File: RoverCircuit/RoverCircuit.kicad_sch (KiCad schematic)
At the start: 0 parts

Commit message: Added Servo and Stepper Motors to circuit schematic
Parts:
- added J1: PIC24_JST_1-10, Connector_JST:JST_EH_B10B-EH-A_1x10_P2.50mm_Vertical, symbol Connector_Generic:Conn_01x10
- added J2: PIC24_JST_11-20, Connector_JST:JST_EH_B10B-EH-A_1x10_P2.50mm_Vertical, symbol Connector_Generic:Conn_01x10
- added J3: Servo_JST, Connector_JST:JST_EH_B3B-EH-A_1x03_P2.50mm_Vertical, symbol Connector_Generic:Conn_01x03
- added J4: Left_Wheel_JST, symbol Connector_Generic:Conn_01x04
- added J5: Right_Wheel_JST, symbol Connector_Generic:Conn_01x04
- added M1: Motor_Servo, symbol Motor:Motor_Servo
- added M2: Left_Wheel, symbol Motor:Stepper_Motor_bipolar
- added M3: Right_Wheel, symbol Motor:Stepper_Motor_bipolar
- added MP1, MP2: MP6500, symbol Custom_Symbol_Library:MP6500_Breakout
- added Q1: NMOS, Package_TO_SOT_THT:TO-92, symbol Simulation_SPICE:NMOS
- added Q2: PMOS, Package_TO_SOT_THT:TO-92, symbol Simulation_SPICE:PMOS
- added R1, R2: 10K, Resistor_THT:R_Axial_DIN0207_L6.3mm_D2.5mm_P10.16mm_Horizontal, symbol Device:R
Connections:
- new net: M2.1, MP1. (4)
- new net: M2.2 (-), MP1. (4)
- new net: M2.3, MP1. (4)
- new net: M2.4, MP1. (4)
- new net: J4.3 (Pin_3), MP1. (4)
- new net: Q2.1 (D), R2.1
- new net: Q1.1 (D), Q2.2 (G), R1.2
- new net: J5.3 (Pin_3), MP2. (4)
- new net: M3.1, MP2. (4)
- new net: M3.2 (-), MP2. (4)
- new net: M3.3, MP2. (4)
- new net: M3.4, MP2. (4)
- new net +3V3: J2.20 (Pin_10)
- new net +5V: J3.1 (Pin_1), J3.2 (Pin_2), M1.1 (PWM), M1.2 (+), Q2.3 (S), R1.1
- new net GND: J2.19 (Pin_9), J3.3 (Pin_3), J4.4 (Pin_4), J5.4 (Pin_4), M1.3 (-), MP1. (4), MP2. (4), Q1.3 (S), R2.2
- new net Left_Wheel_DIR: J2.13 (Pin_3), J4.2 (Pin_2), MP1. (4)
- new net Left_Wheel_Step: J2.11 (Pin_1), J4.1 (Pin_1), MP1. (4)
- new net Right_Wheel_DIR: J2.12 (Pin_2), J5.2 (Pin_2), MP2. (4)
- new net Right_Wheel_Step: J1.4 (Pin_4), J5.1 (Pin_1), MP2. (4)
- new net Servo_PWM: J1.5 (Pin_5), Q1.2 (G)

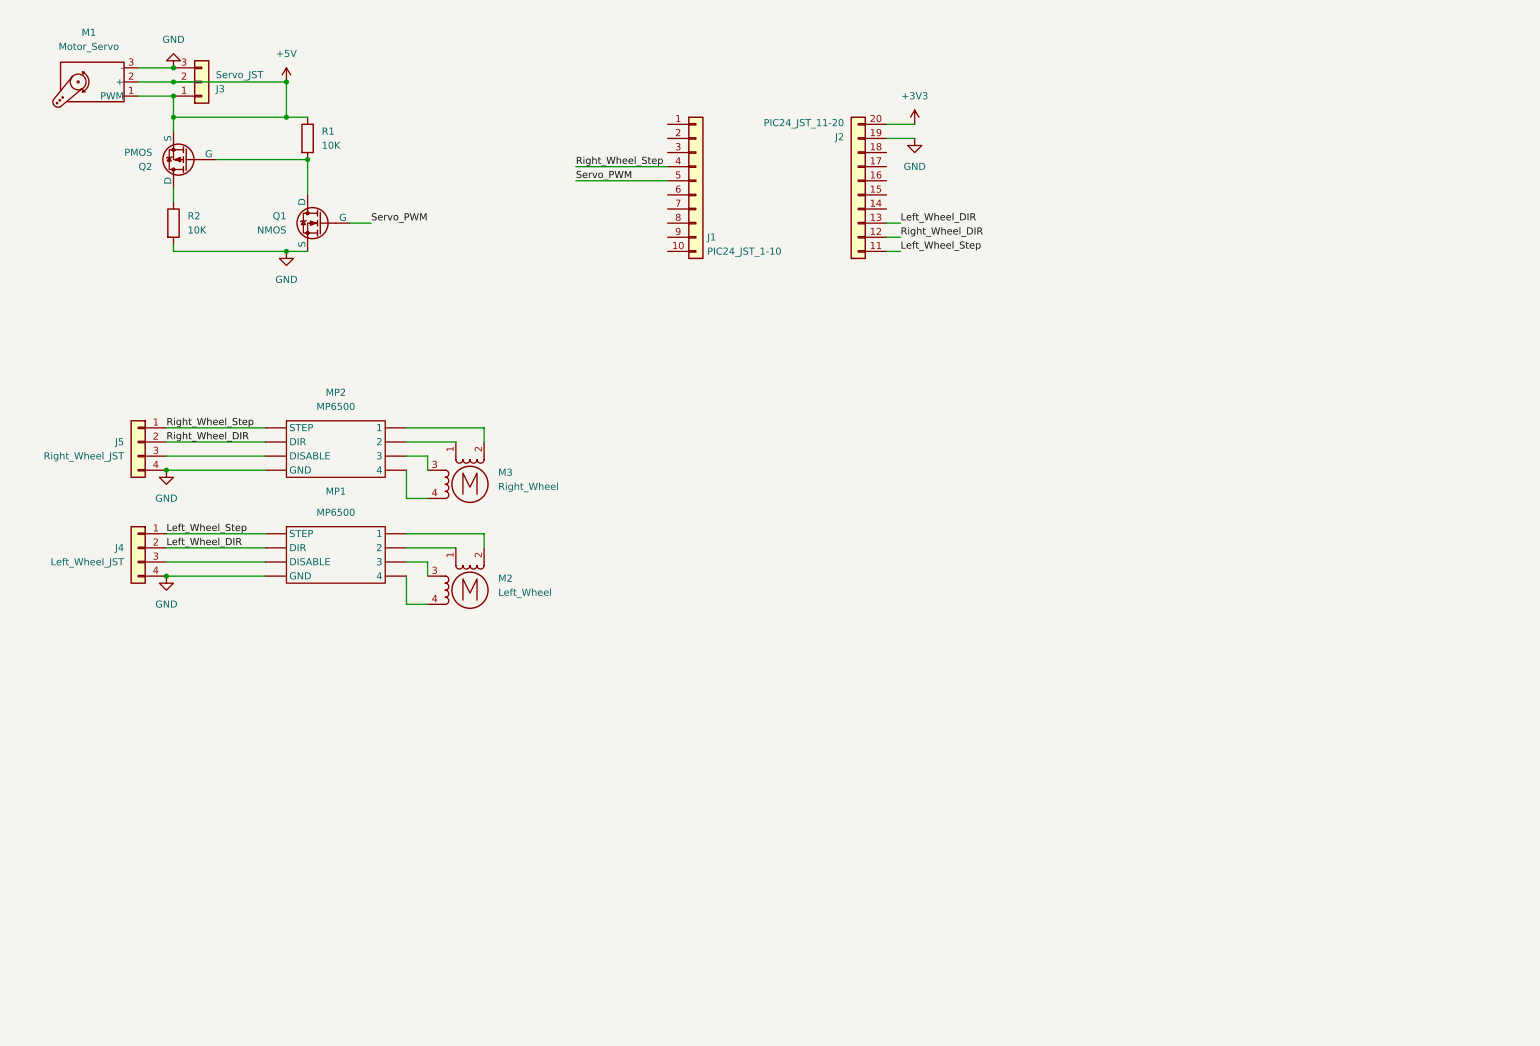
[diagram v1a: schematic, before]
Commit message: Added pinout and voltage rails
Configured pins in MPLAB and added net labels for each pin in KiCad
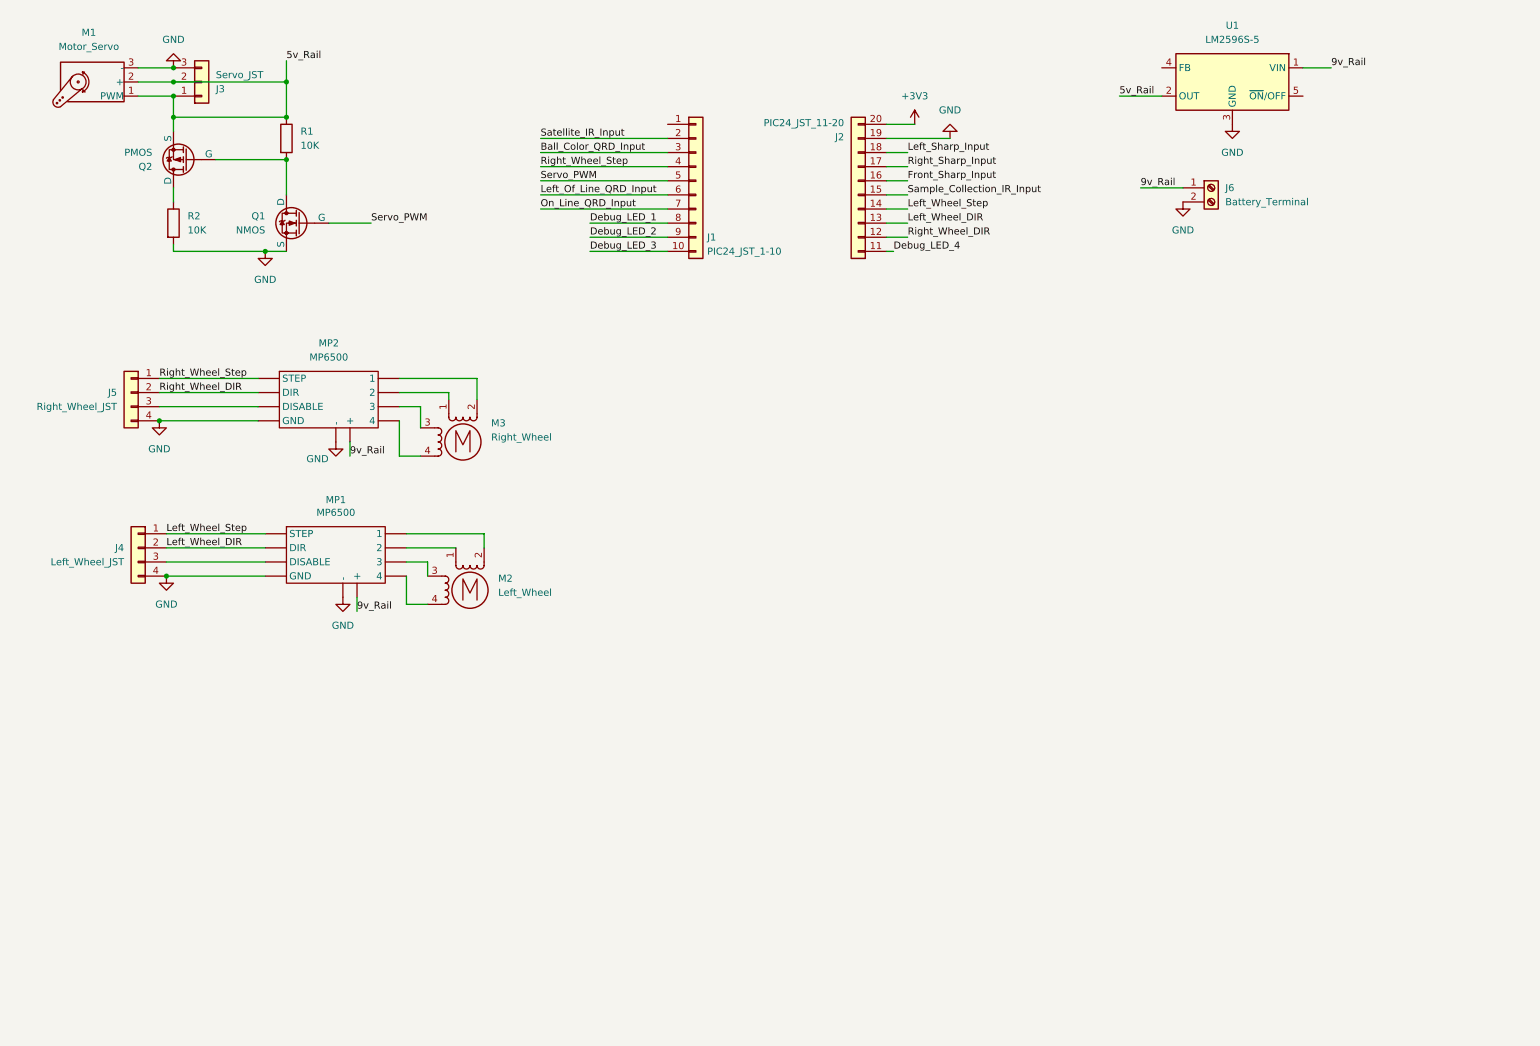
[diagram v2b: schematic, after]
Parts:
- added J6: Battery_Terminal, Connector_Phoenix_SPT:PhoenixContact_SPT_5_1-H-7.5_1x01_P7.5mm_Horizontal, symbol Connector:Screw_Terminal_01x02
- added U1: LM2596S-5, Package_TO_SOT_SMD:TO-263-5_TabPin3, symbol Regulator_Switching:LM2596S-5
- J4, J5: footprint (none) -> Connector_JST:JST_EH_B4B-EH-A_1x04_P2.50mm_Vertical
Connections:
- net GND: now also J6.2 (Pin_2), U1.3 (GND)
- net Left_Wheel_Step: now also J2.14 (Pin_4); no longer J2.11 (Pin_1)
- net Debug_LED_3: now reaches J1.10 (Pin_10)
- net Satellite_IR_Input: now reaches J1.2 (Pin_2)
- net Ball_Color_QRD_Input: now reaches J1.3 (Pin_3)
- net Left_Of_Line_QRD_Input: now reaches J1.6 (Pin_6)
- net On_Line_QRD_Input: now reaches J1.7 (Pin_7)
- net Debug_LED_1: now reaches J1.8 (Pin_8)
- net Debug_LED_2: now reaches J1.9 (Pin_9)
- net Sample_Collection_IR_Input: now reaches J2.15 (Pin_5)
- net Front_Sharp_Input: now reaches J2.16 (Pin_6)
- net Right_Sharp_Input: now reaches J2.17 (Pin_7)
- net Left_Sharp_Input: now reaches J2.18 (Pin_8)
- net +5V renamed 5v_Rail
- net 5v_Rail: now also U1.2 (OUT)
- new net 9v_Rail: J6.1 (Pin_1), MP1. (4), MP2. (4), U1.1 (VIN)
- new net Debug_LED_4: J2.11 (Pin_1)
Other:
- moved on the sheet: J5, M3, Q1, R1

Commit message: Added Sharp Sensors to KiCad
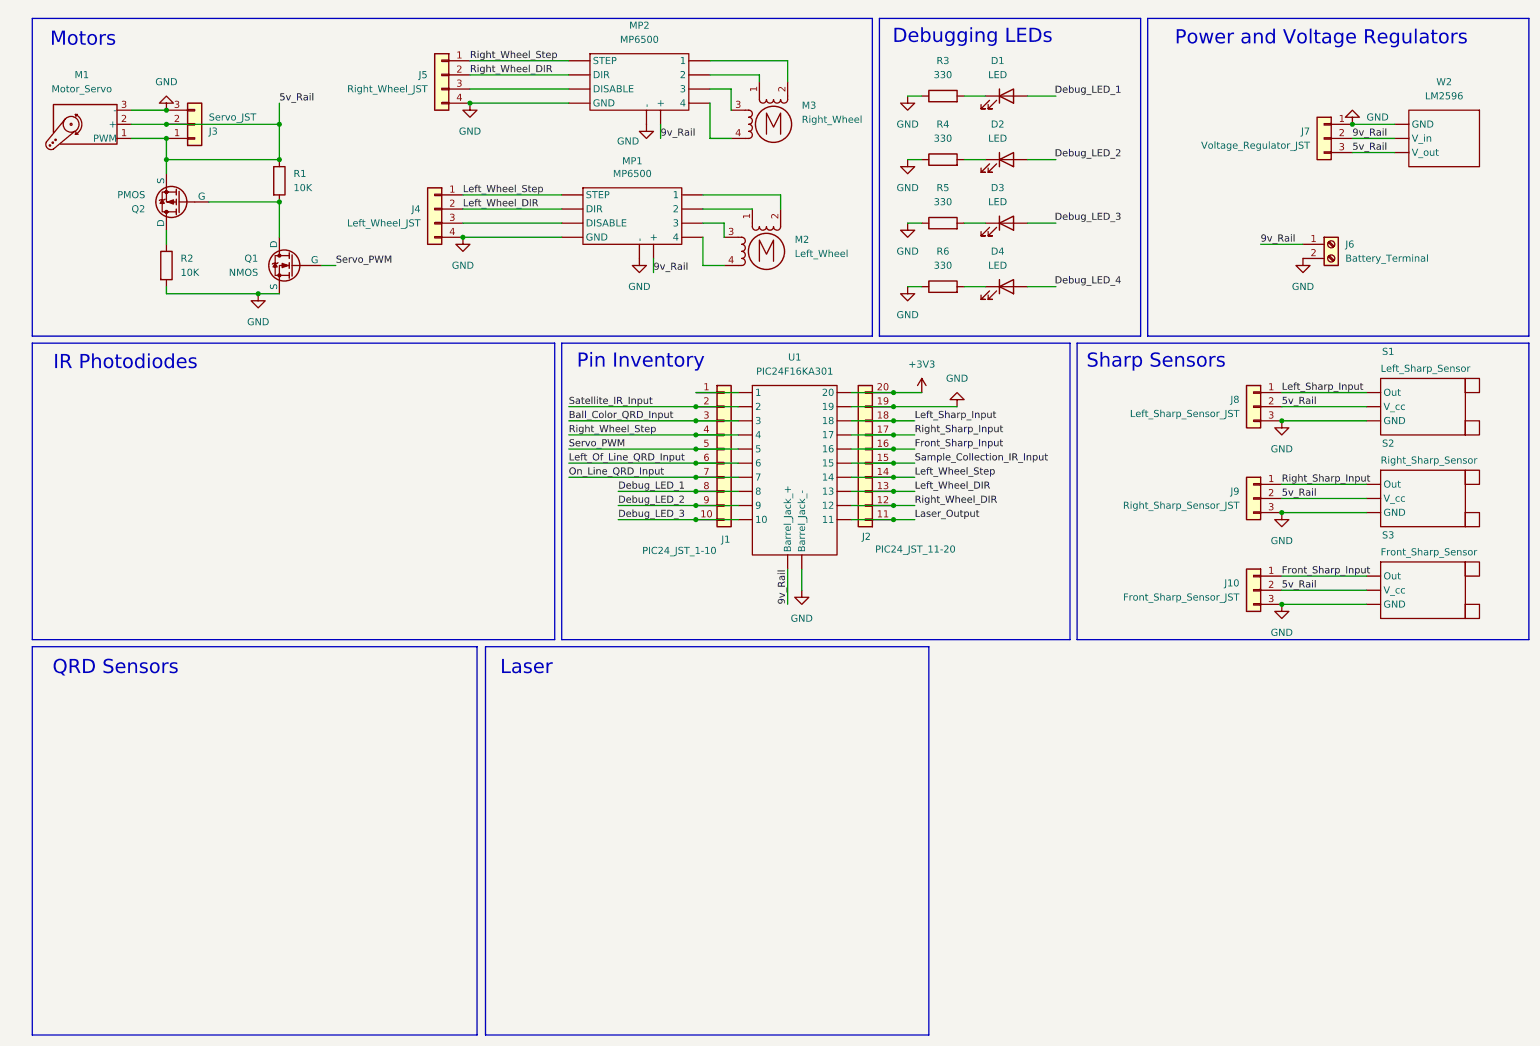
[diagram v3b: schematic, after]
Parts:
- removed U1: LM2596S-5, Package_TO_SOT_SMD:TO-263-5_TabPin3, symbol Regulator_Switching:LM2596S-5
- added D1, D2, D3, D4: LED, LED_THT:LED_D8.0mm, symbol Device:LED
- added J10: Front_Sharp_Sensor_JST, Connector_JST:JST_EH_B3B-EH-A_1x03_P2.50mm_Vertical, symbol Connector_Generic:Conn_01x03
- added J7: Voltage_Regulator_JST, Connector_JST:JST_EH_B3B-EH-A_1x03_P2.50mm_Vertical, symbol Connector_Generic:Conn_01x03
- added J8: Left_Sharp_Sensor_JST, Connector_JST:JST_EH_B3B-EH-A_1x03_P2.50mm_Vertical, symbol Connector_Generic:Conn_01x03
- added J9: Right_Sharp_Sensor_JST, Connector_JST:JST_EH_B3B-EH-A_1x03_P2.50mm_Vertical, symbol Connector_Generic:Conn_01x03
- added R3, R4, R5, R6: 330, Resistor_THT:R_Axial_DIN0207_L6.3mm_D2.5mm_P10.16mm_Horizontal, symbol Device:R
- added S1: Left_Sharp_Sensor, symbol Custom_Symbol_Library:Sharp_Sensor
- added S2: Right_Sharp_Sensor, symbol Custom_Symbol_Library:Sharp_Sensor
- added S3: Front_Sharp_Sensor, symbol Custom_Symbol_Library:Sharp_Sensor
- added U1: PIC24F16KA301, symbol Custom_Symbol_Library:PIC24_Breakout
- added W2: LM2596, symbol Custom_Symbol_Library:LM2596 - 5v Buck Converter
- J6: footprint Connector_Phoenix_SPT:PhoenixContact_SPT_5_1-H-7.5_1x01_P7.5mm_Horizontal -> TerminalBlock_CUI:TerminalBlock_CUI_TB007-508-02_1x02_P5.08mm_Horizontal
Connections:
- net +3V3: now also U1. (11)
- net 5v_Rail: now also J10.2 (Pin_2), J7.3 (Pin_3), J8.2 (Pin_2), J9.2 (Pin_2), S1. (GND), S2. (GND), S3. (GND), W2. (V_out)
- net 9v_Rail: now also J7.2 (Pin_2), U1. (11), W2. (V_out)
- net Ball_Color_QRD_Input: now also U1. (11)
- net Debug_LED_1: now also U1. (11)
- net Debug_LED_2: now also U1. (11)
- net Debug_LED_3: now also U1. (11)
- net Debug_LED_4: no longer J2.11 (Pin_1)
- net Front_Sharp_Input: now also J10.1 (Pin_1), S3. (GND), U1. (11)
- net GND: now also J10.3 (Pin_3), J7.1 (Pin_1), J8.3 (Pin_3), J9.3 (Pin_3), R3.1, R4.1, R5.1, R6.1, S1. (GND), S2. (GND), S3. (GND), U1. (11), W2. (V_out)
- net Left_Of_Line_QRD_Input: now also U1. (11)
- net Left_Sharp_Input: now also J8.1 (Pin_1), S1. (GND), U1. (11)
- net Left_Wheel_DIR: now also U1. (11)
- net Left_Wheel_Step: now also U1. (11)
- net On_Line_QRD_Input: now also U1. (11)
- net Right_Sharp_Input: now also J9.1 (Pin_1), S2. (GND), U1. (11)
- net Right_Wheel_DIR: now also U1. (11)
- net Right_Wheel_Step: now also U1. (11)
- net Sample_Collection_IR_Input: now also U1. (11)
- net Satellite_IR_Input: now also U1. (11)
- net Servo_PWM: now also U1. (11)
- net at J1.1 (Pin_1): now also U1. (11)
- new net: D3.1 (K), R5.2
- new net: D1.1 (K), R3.2
- new net: D4.1 (K), R6.2
- new net: D2.1 (K), R4.2
- new net Laser_Output: J2.11 (Pin_1), U1. (11)
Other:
- note added: "Debugging LEDs"
- note added: "IR Photodiodes"
- note added: "Laser"
- note added: "Motors"
- note added: "Pin Inventory"
- note added: "Power and Voltage Regulators"
- note added: "QRD Sensors"
- note added: "Sharp Sensors"
- moved on the sheet: J1, J2, J3, J4, J5, J6, M1, M2, M3, MP1, MP2, Q1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

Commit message: Finalized rover circuit schematic, first version of QRD circuit
rover circuit layout and traces not finished yet
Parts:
- removed D3, D4: LED, LED_THT:LED_D8.0mm, symbol Device:LED
- removed R5: 330, Resistor_THT:R_Axial_DIN0207_L6.3mm_D2.5mm_P10.16mm_Horizontal, symbol Device:R
- added C1, C2: 0.1uF, Capacitor_THT:C_Disc_D3.4mm_W2.1mm_P2.50mm, symbol Device:C
- added D4: Sample_Photodiode, symbol Device:D_Photo
- added D5: Satellite_Photodiode, symbol Device:D_Photo
- added J10: JST_5Pin_P2.54_H, Connector_JST:JST_EH_S5B-EH_1x05_P2.50mm_Horizontal, symbol Connector_Generic:Conn_01x05
- added J11_Sample_IR_Diode1, J12_Satellite_IR_Diode1, J13_Laser1: JST_2Pin_P2.54_V, Connector_JST:JST_EH_B2B-EH-A_1x02_P2.50mm_Vertical, symbol Connector_Generic:Conn_01x02
- added J14_QRD_Board1: JST_5Pin_P2.54_V, Connector_JST:JST_EH_B5B-EH-A_1x05_P2.50mm_Vertical, symbol Connector_Generic:Conn_01x05
- added LD1: D_Laser_1C2A, symbol Device:D_Laser_1C2A
- added Left_Wheel1: Left_Wheel_Power_Terminal, Custom_Library:screw_terminal, symbol Connector:Screw_Terminal_01x02
- added PIC_Barrel_Jack1: PIC_Power_Terminal, Custom_Library:screw_terminal, symbol Connector:Screw_Terminal_01x02
- added Q3, Q4, Q5: QRD1114, Diode_THT:Diode_Bridge_DIP-4_W5.08mm_P2.54mm, symbol Custom_Symbol_Library:_1
- added Q6: NMOS, Package_TO_SOT_THT:TO-92, symbol Simulation_SPICE:NMOS
- added R10, R8, R9: 330Ω, Resistor_THT:R_Axial_DIN0207_L6.3mm_D2.5mm_P10.16mm_Horizontal, symbol Device:R
- added R11, R12, R13, R14: 10kΩ, Resistor_THT:R_Axial_DIN0207_L6.3mm_D2.5mm_P10.16mm_Horizontal, symbol Device:R
- added R7: 1MΩ, Resistor_THT:R_Axial_DIN0207_L6.3mm_D2.5mm_P10.16mm_Horizontal, symbol Device:R
- added Right_Wheel1: Right_Wheel_Terminal, Custom_Library:screw_terminal, symbol Connector:Screw_Terminal_01x02
- added SW1: SW_SPST, symbol Switch:SW_SPST
- added U2: LM1117T-3.3, Package_TO_SOT_THT:TO-220-3_Horizontal_TabDown, symbol Regulator_Linear:LM1117T-3.3
- added U3: LM324, Package_DIP:DIP-14_W7.62mm, symbol Amplifier_Operational:LM324
- Battery1: renamed from J6; footprint TerminalBlock_CUI:TerminalBlock_CUI_TB007-508-02_1x02_P5.08mm_Horizontal -> Custom_Library:screw_terminal
- J1_Servo1: renamed from J3; value Servo_JST -> JST_3Pin_P2.54_V
- J2_Left_Wheel1: renamed from J4; value Left_Wheel_JST -> JST_4Pin_P2.54_V
- J3_Right_Wheel1: renamed from J5; value Right_Wheel_JST -> JST_4Pin_P2.54_V
- J4: renamed from J1; value PIC24_JST_1-10 -> JST_10Pin_P2.54_V
- J5: renamed from J2; value PIC24_JST_11-20 -> JST_10Pin_P2.54_V
- J6_Left_Sharp1: renamed from J8; value Left_Sharp_Sensor_JST -> JST_3Pin_P2.54_V
- J7_Right_Sharp1: renamed from J9; value Right_Sharp_Sensor_JST -> JST_3Pin_P2.54_V
- J8_Front_Sharp1: renamed from J10; value Front_Sharp_Sensor_JST -> JST_3Pin_P2.54_V
- J9_5v_Regulator1: renamed from J7; value Voltage_Regulator_JST -> JST_3Pin_P2.54_V
- R6: value 330 -> 1MΩ
- renumbered Q2 to Q1, Q1 to Q2, R2 to R1, R1 to R2, W2 to W1
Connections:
- net 5v_Rail: now also U2.3 (VI)
- net Debug_LED_1: now also J4.9 (Pin_9); no longer J4.8 (Pin_8)
- net Debug_LED_2: now also J4.10 (Pin_10); no longer J4.9 (Pin_9)
- net GND: now also D4.2 (A), D5.2 (A), J10.1 (Pin_1), J11_Sample_IR_Diode1.2 (Pin_2), J12_Satellite_IR_Diode1.2 (Pin_2), J14_QRD_Board1.1 (Pin_1), Left_Wheel1.2 (Pin_2), PIC_Barrel_Jack1.2 (Pin_2), Q3.2 (GND), Q3.4 (GND), Q4.2 (GND), Q4.4 (GND), Q5.2 (GND), Q5.4 (GND), Q6.3 (S), R14.1, Right_Wheel1.2 (Pin_2), U2.1 (GND), U3.11 (V-), U3.3 (+), U3.6 (-); no longer R6.1
- net Laser_Output: now also Q6.2 (G), R14.2
- net Left_Of_Line_QRD_Input: now also J10.5 (Pin_5), J14_QRD_Board1.5 (Pin_5), Q5.1 (Out), R11.1
- net On_Line_QRD_Input: now also J10.4 (Pin_4), J14_QRD_Board1.4 (Pin_4), Q4.1 (Out), R12.1
- net Sample_Collection_IR_Input: now also R6.2, C1.2, U3.1
- net Satellite_IR_Input: now also C2.2, R7.2, U3.7
- net +3V3: no longer names the net of J5.20 (Pin_10), U1. (11)
- removed net 9v_Rail: Battery1.1 (Pin_1), J9_5v_Regulator1.2 (Pin_2), MP1. (4), MP2. (4), U1. (11), W1. (V_out)
- removed net Debug_LED_3: J4.10 (Pin_10), U1. (11)
- new net: Q5.3 (Vin), R10.2
- new net: C1.1, D4.1 (K), J11_Sample_IR_Diode1.1 (Pin_1), R6.1, U3.2 (-)
- new net: C2.1, D5.1 (K), J12_Satellite_IR_Diode1.1 (Pin_1), R7.1, U3.5 (+)
- new net: Q3.3 (Vin), R8.2
- new net: J13_Laser1.2 (Pin_2), LD1.1 (K), Q6.1 (D)
- new net: Q4.3 (Vin), R9.2
- new net: Battery1.1 (Pin_1), SW1.1 (A)
- new net 12v_Rail: J9_5v_Regulator1.2 (Pin_2), Left_Wheel1.1 (Pin_1), MP1. (4), MP2. (4), PIC_Barrel_Jack1.1 (Pin_1), Right_Wheel1.1 (Pin_1), SW1.2 (B), U1. (11), W1. (V_out)
- new net 3.3v_Rail: J10.2 (Pin_2), J13_Laser1.1 (Pin_1), J14_QRD_Board1.2 (Pin_2), LD1.2 (A), R10.1, R11.2, R12.2, R13.2, R8.1, R9.1, U2.2 (VO), U3.4 (V+)
- new net Right_Of_Line_QRD_Input: J10.3 (Pin_3), J14_QRD_Board1.3 (Pin_3), J4.8 (Pin_8), Q3.1 (Out), R13.1, U1. (11)
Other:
- moved on the sheet: Battery1, D1, D2, J2_Left_Wheel1, J3_Right_Wheel1, J9_5v_Regulator1, M2, M3, MP1, MP2, R3, R4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
